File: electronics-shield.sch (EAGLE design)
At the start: 72 parts, among them IC1 TLE9201SG, IC2 TLE9201SG, IC3 TLE9201SG, IC4 TLE9201SG, Q2 IRFR5305, U1 STM32F0XX8T, U4 V_REG_317SMD, X1 CONNECTOR_PHOENIX_3.81, X2 Listwa zaciskowa rozłączalna 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, Y2 8MHz

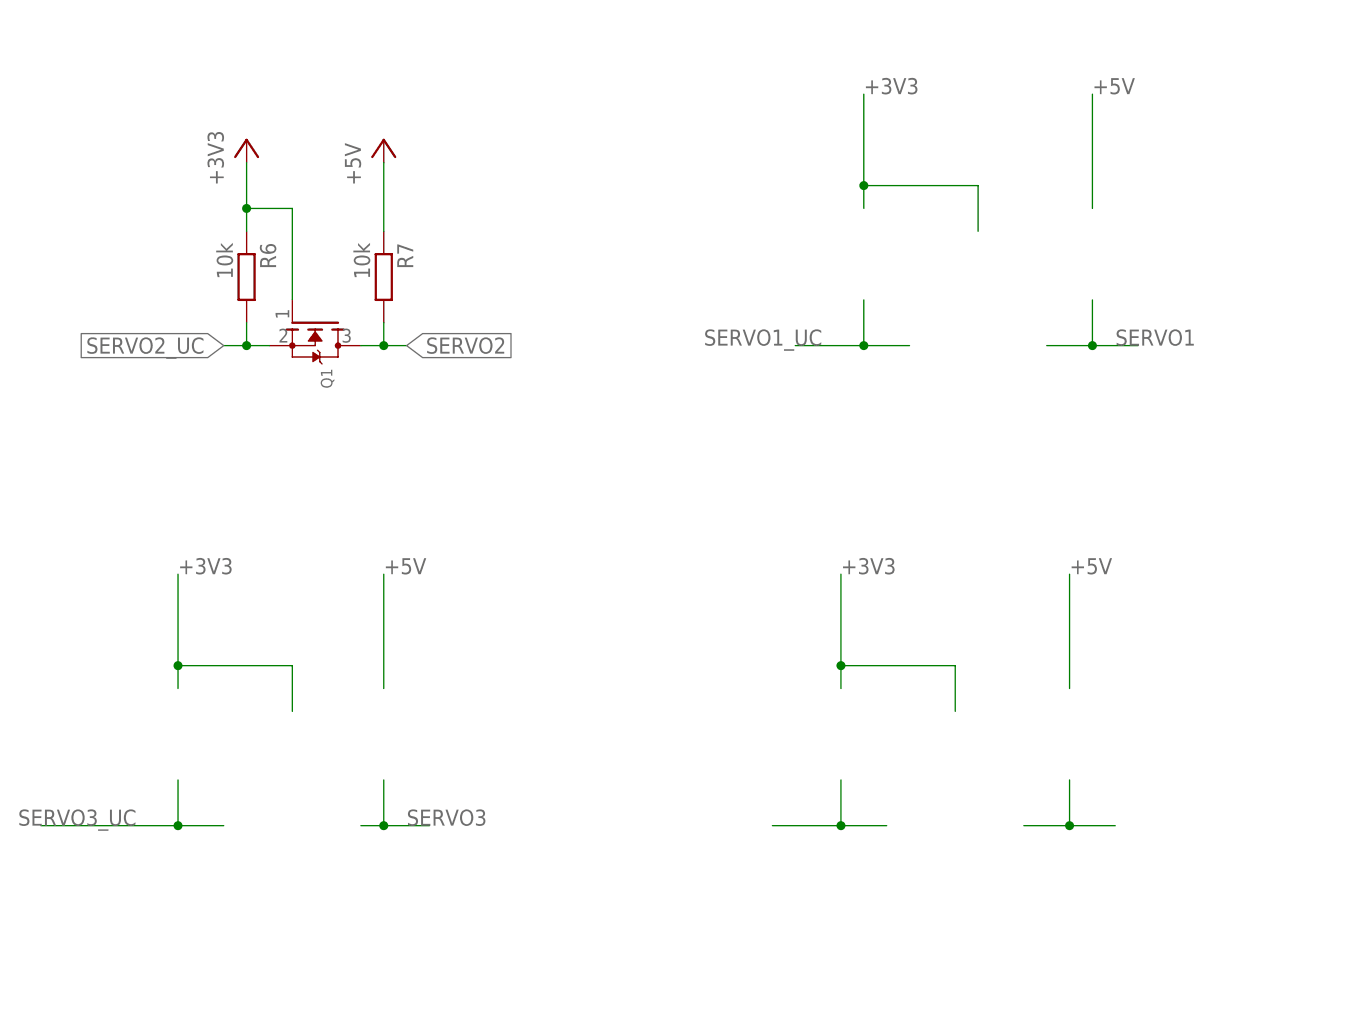
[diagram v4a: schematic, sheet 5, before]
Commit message: Basic placement of rest of components
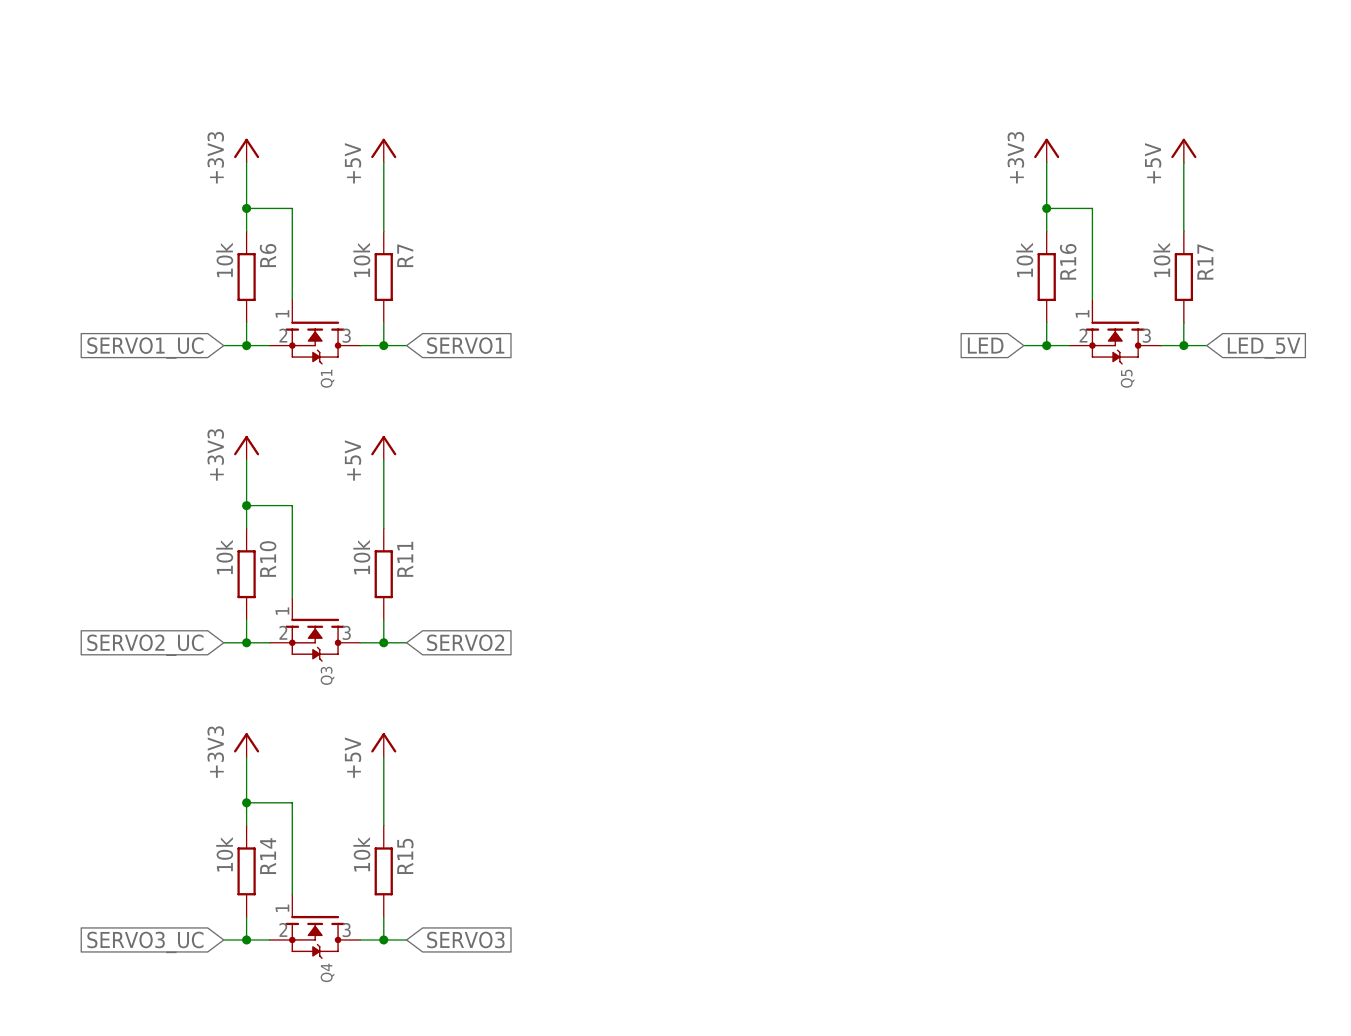
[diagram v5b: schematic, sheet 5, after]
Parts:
- removed LED4, LED5: LEDCHIPLED_0603, audio amplifier example:LEDCHIPLED_0603
- added JP4: (no value), pinhead:PINHD-1X3
- added Q3, Q4, Q5: (no value), adafruit:MOSFET-NREFLOW
- added R10, R11, R14, R15, R16, R17: 10k, rcl:R-EU_R0603
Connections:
- net DATA_N renamed NSS_1
- net DATA_P renamed NSS_2
- removed net N$4: LED4.C, R12.1
- removed net N$5: LED5.C, R13.1
- removed net SO1-SI3: IC1.SO, IC3.SI
- removed net SO2-SI4: IC2.SO, IC4.SI
- removed net SO3-SI2: IC2.SI, IC3.SO
- new net LED_5V: JP4.1, Q5.D, R17.2
- net +3V3: now also Q3.G, Q4.G, Q5.G, R10.1, R14.1, R16.1; no longer LED5.A
- net +5V: now also R11.1, R15.1, R17.1; no longer LED4.A
- net BAT_MEAS: now also R12.2, R13.1
- net GND: now also IC1.CS_N, IC1.SCK, IC1.SI, IC1.SO, IC2.CS_N, IC2.SCK, IC2.SI, IC2.SO, IC3.CS_N, IC3.SCK, IC3.SI, IC3.SO, IC4.CS_N, IC4.SCK, IC4.SI, IC4.SO, JP4.3; no longer R12.2
- net LED: now also Q5.S, R16.2
- net RPI_CLK: no longer IC1.SCK, IC2.SCK, IC3.SCK, IC4.SCK
- net RPI_MISO: no longer IC4.SO
- net RPI_MOSI: no longer IC1.SI
- net SERVO1: now also Q1.D, R7.2
- net SERVO1_UC: now also Q1.S, R6.2
- net SERVO2: now also Q3.D, R11.2; no longer Q1.D, R7.2
- net SERVO2_UC: now also Q3.S, R10.2; no longer Q1.S, R6.2
- net SERVO3: now also Q4.D, R15.2
- net SERVO3_UC: now also Q4.S, R14.2
- net TLE_NSS: no longer IC1.CS_N, IC2.CS_N, IC3.CS_N, IC4.CS_N
- net VCC: now also JP4.2, R12.1
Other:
- note removed: "I2C2"

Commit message: Finish wiring, DRC done
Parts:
- added U2, U3: NC7SV157P6X, Kell Ideas:NC7SV157P6X
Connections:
- removed net SCL: PCB1.GPIO03/SCL1, R3.1
- removed net SDA: PCB1.GPIO02/SDA1, R2.1
- net +3V3: now also U2.VCC, U3.VCC
- net GND: now also U2.GND, U3.GND
- net NSS_1: now also PCB1.!CE0!/GPIO08, U1PA.PA15
- net RPI_RXD: now also U3.Z
- net RPI_TXD: now also U2.Z
- net SCL_TX: now also PCB1.GPIO03/SCL1, R3.1, U2.I1; no longer U1PB.PB10
- net SDA_RX: now also PCB1.GPIO02/SDA1, R2.1, U3.I1; no longer U1PB.PB11
- net SIGNAL_SELECTOR: now also U2.S, U3.S
- net SPI1_NSS: no longer PCB1.!CE0!/GPIO08, U1PA.PA15
- net STM_RX: now also U2.I0
- net STM_TX: now also U3.I0
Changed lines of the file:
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@@
 <part name="GND34" library="supply1" library_urn="urn:adsk.eagle:library:371" deviceset="GND" device=""/>
 <part name="GND35" library="supply1" library_urn="urn:adsk.eagle:library:371" deviceset="GND" device=""/>
+<part name="U2" library="Kell Ideas" library_urn="urn:adsk.eagle:library:4431361" deviceset="NC7SV157P6X" device="" package3d_urn="urn:adsk.eagle:package:8973299/1"/>
+<part name="U3" library="Kell Ideas" library_urn="urn:adsk.eagle:library:4431361" deviceset="NC7SV157P6X" device="" package3d_urn="urn:adsk.eagle:package:8973299/1"/>
+<part name="+3V10" library="supply1" library_urn="urn:adsk.eagle:library:371" deviceset="+3V3" device=""/>
+<part name="+3V11" library="supply1" library_urn="urn:adsk.eagle:library:371" deviceset="+3V3" device=""/>
+<part name="GND42" library="supply1" library_urn="urn:adsk.eagle:library:371" deviceset="GND" device=""/>
+<part name="GND43" library="supply1" library_urn="urn:adsk.eagle:library:371" deviceset="GND" device=""/>
 </parts>
 <sheets>
@@
 </segment>
 </net>
-<net name="SDA" class="0">
-<segment>
-<pinref part="R2" gate="&gt;NAME" pin="1"/>
-<wire x1="35.56" y1="137.16" x2="38.1" y2="137.16" width="0.1524" layer="91"/>
-<label x="38.1" y="137.16" size="0.8128" layer="95" rot="MR180" xref="yes"/>
-</segment>
-</net>
-<net name="SCL" class="0">
-<segment>
-<pinref part="R3" gate="&gt;NAME" pin="1"/>
-<wire x1="38.1" y1="127" x2="35.56" y2="127" width="0.1524" layer="91"/>
-<label x="38.1" y="127" size="0.8128" layer="95" rot="MR180" xref="yes"/>
-</segment>
-</net>
 <net name="+3V3" class="3">
 <segment>
@@
 <net name="SPI1_NSS" class="0">
 <segment>
-<wire x1="96.52" y1="121.92" x2="99.06" y2="121.92" width="0.1524" layer="91"/>
-<label x="99.06" y="121.92" size="0.8128" layer="95" xref="yes"/>
-<pinref part="U1" gate="PA" pin="PA15"/>
-</segment>
-<segment>
 <pinref part="R1" gate="&gt;NAME" pin="1"/>
 <wire x1="35.56" y1="147.32" x2="38.1" y2="147.32" width="0.1524" layer="91"/>
@@
 <net name="SCL_TX" class="0">
 <segment>
-<wire x1="93.98" y1="63.5" x2="99.06" y2="63.5" width="0.1524" layer="91"/>
-<label x="99.06" y="63.5" size="0.8128" layer="95" xref="yes"/>
-<pinref part="U1" gate="PB" pin="PB10"/>
+<pinref part="R3" gate="&gt;NAME" pin="1"/>
+<wire x1="38.1" y1="127" x2="35.56" y2="127" width="0.1524" layer="91"/>
+<label x="38.1" y="127" size="0.8128" layer="95" rot="MR180" xref="yes"/>
 </segment>
 </net>
 <net name="SDA_RX" class="0">
 <segment>
-<wire x1="93.98" y1="60.96" x2="99.06" y2="60.96" width="0.1524" layer="91"/>
-<label x="99.06" y="60.96" size="0.8128" layer="95" xref="yes"/>
-<pinref part="U1" gate="PB" pin="PB11"/>
+<pinref part="R2" gate="&gt;NAME" pin="1"/>
+<wire x1="35.56" y1="137.16" x2="38.1" y2="137.16" width="0.1524" layer="91"/>
+<label x="38.1" y="137.16" size="0.8128" layer="95" rot="MR180" xref="yes"/>
 </segment>
 </net>
@@
 <label x="99.06" y="71.12" size="0.8128" layer="95" xref="yes"/>
 <pinref part="U1" gate="PB" pin="PB7"/>
+</segment>
+</net>
+<net name="NSS_1" class="5">
+<segment>
+<wire x1="96.52" y1="121.92" x2="99.06" y2="121.92" width="0.1524" layer="91"/>
+<label x="99.06" y="121.92" size="0.8128" layer="95" xref="yes"/>
+<pinref part="U1" gate="PA" pin="PA15"/>
 </segment>
 </net>
@@
 </segment>
 </net>
-<net name="SDA" class="0">
+<net name="SDA_RX" class="0">
 <segment>
 <wire x1="111.76" y1="124.46" x2="106.68" y2="124.46" width="0.1524" layer="91"/>
@@
 </segment>
 </net>
-<net name="SCL" class="0">
+<net name="SCL_TX" class="0">
 <segment>
 <wire x1="111.76" y1="121.92" x2="106.68" y2="121.92" width="0.1524" layer="91"/>
@@
 <label x="165.1" y="101.6" size="0.8128" layer="95" rot="MR180" xref="yes"/>
 <pinref part="PCB1" gate="G$1" pin="GEN6/GPIO25"/>
-</segment>
-</net>
-<net name="SPI1_NSS" class="0">
-<segment>
-<wire x1="152.4" y1="99.06" x2="165.1" y2="99.06" width="0.1524" layer="91"/>
-<label x="165.1" y="99.06" size="0.8128" layer="95" rot="MR180" xref="yes"/>
-<pinref part="PCB1" gate="G$1" pin="!CE0!/GPIO08"/>
 </segment>
 </net>
@@
 <pinref part="F3" gate="G$1" pin="1"/>
 <wire x1="167.64" y1="127" x2="175.26" y2="127" width="0.1524" layer="91"/>
+</segment>
+</net>
+<net name="NSS_1" class="5">
+<segment>
+<wire x1="152.4" y1="99.06" x2="165.1" y2="99.06" width="0.1524" layer="91"/>
+<label x="165.1" y="99.06" size="0.8128" layer="95" rot="MR180" xref="yes"/>
+<pinref part="PCB1" gate="G$1" pin="!CE0!/GPIO08"/>
 </segment>
 </net>
@@
 <attribute name="CREVISION" x="252.7" y="1.17" size="2.54" layer="94" font="vector"/>
 </instance>
+<instance part="U2" gate="A" x="101.6" y="147.32" smashed="yes">
+<attribute name="NAME" x="96.05701875" y="160.0587" size="2.08496875" layer="95" ratio="10" rot="SR0"/>
+<attribute name="VALUE" x="98.06498125" y="125.1943" size="2.085409375" layer="96" ratio="10" rot="SR0"/>
+</instance>
+<instance part="U3" gate="A" x="101.6" y="109.22" smashed="yes">
+<attribute name="NAME" x="96.05701875" y="121.9587" size="2.08496875" layer="95" ratio="10" rot="SR0"/>
+<attribute name="VALUE" x="98.06498125" y="87.0943" size="2.085409375" layer="96" ratio="10" rot="SR0"/>
+</instance>
+<instance part="+3V10" gate="G$1" x="81.28" y="160.02" smashed="yes">
+<attribute name="VALUE" x="78.74" y="154.94" size="1.778" layer="96" rot="R90"/>
+</instance>
+<instance part="+3V11" gate="G$1" x="81.28" y="119.38" smashed="yes">
+<attribute name="VALUE" x="78.74" y="114.3" size="1.778" layer="96" rot="R90"/>
+</instance>
+<instance part="GND42" gate="1" x="81.28" y="129.54" smashed="yes">
+<attribute name="VALUE" x="78.74" y="127" size="1.778" layer="96"/>
+</instance>
+<instance part="GND43" gate="1" x="81.28" y="91.44" smashed="yes">
+<attribute name="VALUE" x="78.74" y="88.9" size="1.778" layer="96"/>
+</instance>
 </instances>
 <busses>
 </busses>
 <nets>
+<net name="SDA_RX" class="0">
+<segment>
+<pinref part="U3" gate="A" pin="I1"/>
+<wire x1="83.82" y1="109.22" x2="81.28" y2="109.22" width="0.1524" layer="91"/>
+<label x="81.28" y="109.22" size="1.27" layer="95" rot="R180" xref="yes"/>
+</segment>
+</net>
+<net name="STM_TX" class="0">
+<segment>
+<pinref part="U3" gate="A" pin="I0"/>
+<wire x1="83.82" y1="106.68" x2="81.28" y2="106.68" width="0.1524" layer="91"/>
+<label x="81.28" y="106.68" size="1.27" layer="95" rot="R180" xref="yes"/>
+</segment>
+</net>
+<net name="SIGNAL_SELECTOR" class="0">
+<segment>
+<pinref part="U2" gate="A" pin="S"/>
+<wire x1="83.82" y1="139.7" x2="81.28" y2="139.7" width="0.1524" layer="91"/>
+<label x="81.28" y="139.7" size="1.27" layer="95" rot="R180" xref="yes"/>
+</segment>
+<segment>
+<pinref part="U3" gate="A" pin="S"/>
+<wire x1="83.82" y1="101.6" x2="81.28" y2="101.6" width="0.1524" layer="91"/>
+<label x="81.28" y="101.6" size="1.27" layer="95" rot="R180" xref="yes"/>
+</segment>
+</net>
+<net name="SCL_TX" class="0">
+<segment>
+<pinref part="U2" gate="A" pin="I1"/>
+<wire x1="83.82" y1="147.32" x2="81.28" y2="147.32" width="0.1524" layer="91"/>
+<label x="81.28" y="147.32" size="1.27" layer="95" rot="R180" xref="yes"/>
+</segment>
+</net>
+<net name="+3V3" class="3">
+<segment>
+<pinref part="U2" gate="A" pin="VCC"/>
+<wire x1="83.82" y1="152.4" x2="81.28" y2="152.4" width="0.1524" layer="91"/>
+<wire x1="81.28" y1="152.4" x2="81.28" y2="157.48" width="0.1524" layer="91"/>
+<pinref part="+3V10" gate="G$1" pin="+3V3"/>
+</segment>
+<segment>
+<pinref part="U3" gate="A" pin="VCC"/>
+<wire x1="83.82" y1="114.3" x2="81.28" y2="114.3" width="0.1524" layer="91"/>
+<wire x1="81.28" y1="114.3" x2="81.28" y2="116.84" width="0.1524" layer="91"/>
+<pinref part="+3V11" gate="G$1" pin="+3V3"/>
+</segment>
+</net>
+<net name="GND" class="2">
+<segment>
+<pinref part="U2" gate="A" pin="GND"/>
+<wire x1="83.82" y1="134.62" x2="81.28" y2="134.62" width="0.1524" layer="91"/>
+<wire x1="81.28" y1="134.62" x2="81.28" y2="132.08" width="0.1524" layer="91"/>
+<pinref part="GND42" gate="1" pin="GND"/>
+</segment>
+<segment>
+<pinref part="U3" gate="A" pin="GND"/>
+<wire x1="83.82" y1="96.52" x2="81.28" y2="96.52" width="0.1524" layer="91"/>
+<wire x1="81.28" y1="96.52" x2="81.28" y2="93.98" width="0.1524" layer="91"/>
+<pinref part="GND43" gate="1" pin="GND"/>
+</segment>
+</net>
+<net name="RPI_TXD" class="0">
+<segment>
+<pinref part="U2" gate="A" pin="Z"/>
+<wire x1="119.38" y1="152.4" x2="121.92" y2="152.4" width="0.1524" layer="91"/>
+<label x="121.92" y="152.4" size="1.27" layer="95" xref="yes"/>
+</segment>
+</net>
+<net name="RPI_RXD" class="0">
+<segment>
+<pinref part="U3" gate="A" pin="Z"/>
+<wire x1="119.38" y1="114.3" x2="121.92" y2="114.3" width="0.1524" layer="91"/>
+<label x="121.92" y="114.3" size="1.27" layer="95" xref="yes"/>
+</segment>
+</net>
+<net name="STM_RX" class="0">
+<segment>
+<pinref part="U2" gate="A" pin="I0"/>
+<wire x1="83.82" y1="144.78" x2="81.28" y2="144.78" width="0.1524" layer="91"/>
+<label x="81.28" y="144.78" size="1.27" layer="95" rot="R180" xref="yes"/>
+</segment>
+</net>
 </nets>
 </sheet>
